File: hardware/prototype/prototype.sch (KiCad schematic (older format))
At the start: 75 parts, among them J1 0734120114, J2 Conn_01x04, J4 Conn_01x04, J5 Conn_02x07_Odd_Even, J6 Battery-holder, J7 Conn_02x12_Odd_Even, J8 Jack-DC, Q1 DTC143Z, Q2 Si2323, U1 QUECTEL_L80, U2 TLV71333PDBV, U3 LM2596_MODULE, U4 DevkitC, U5 MIKROE_3G_CLICK

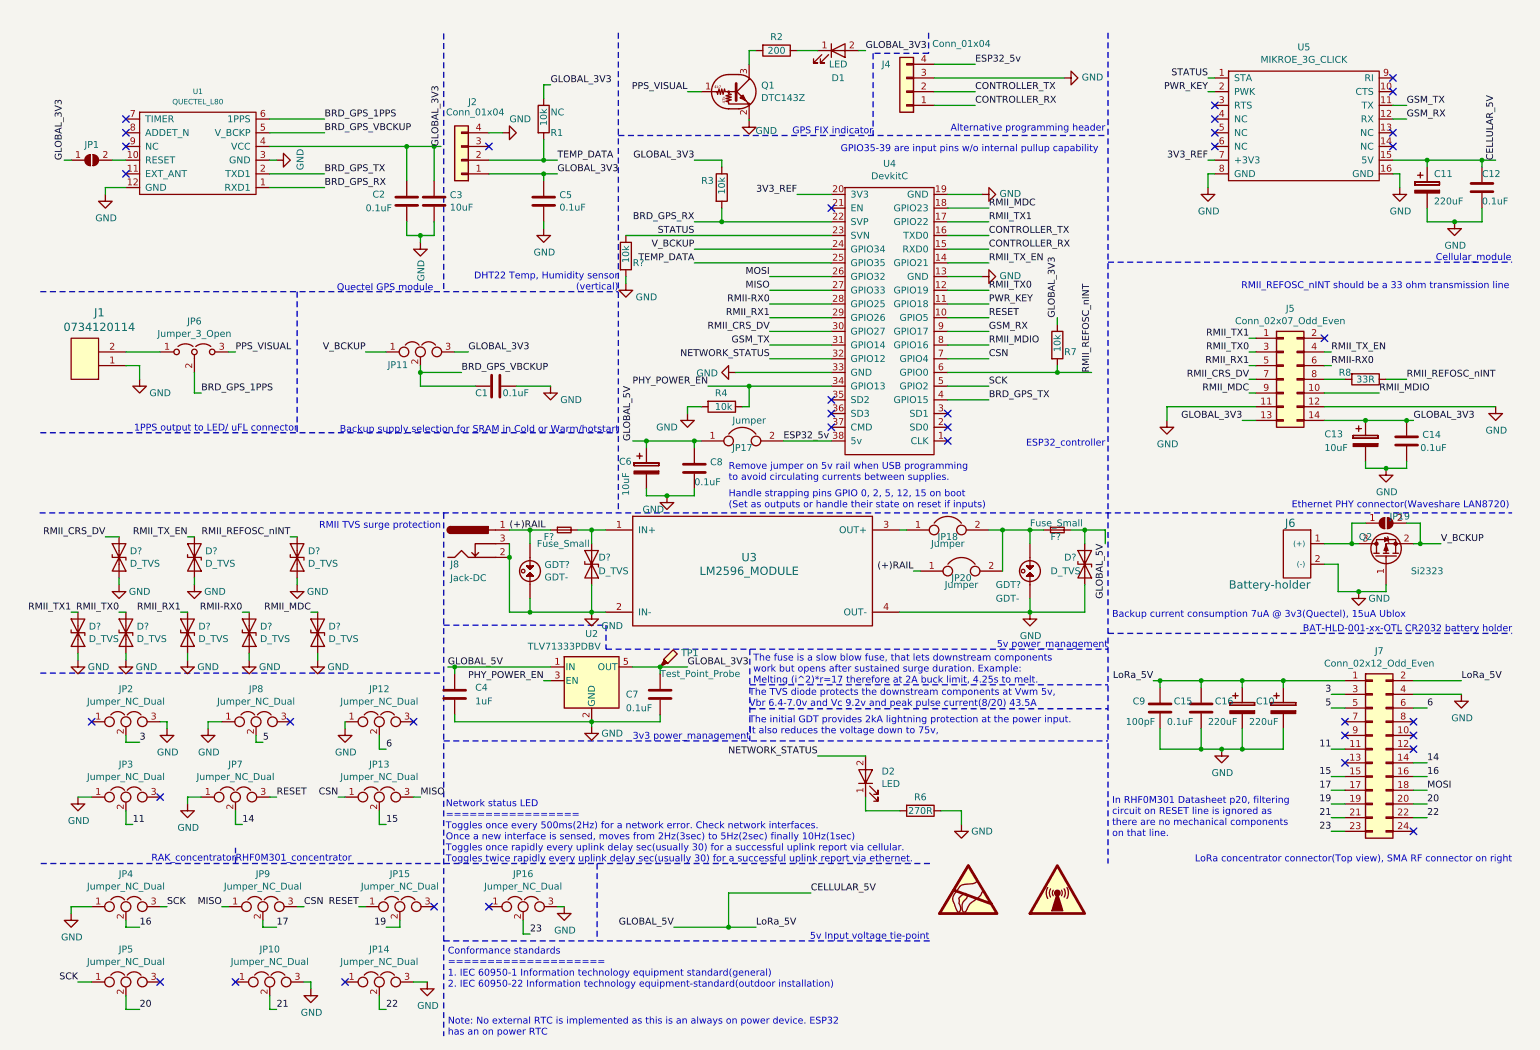
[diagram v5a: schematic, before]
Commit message: Complete schematic and component footpint selection
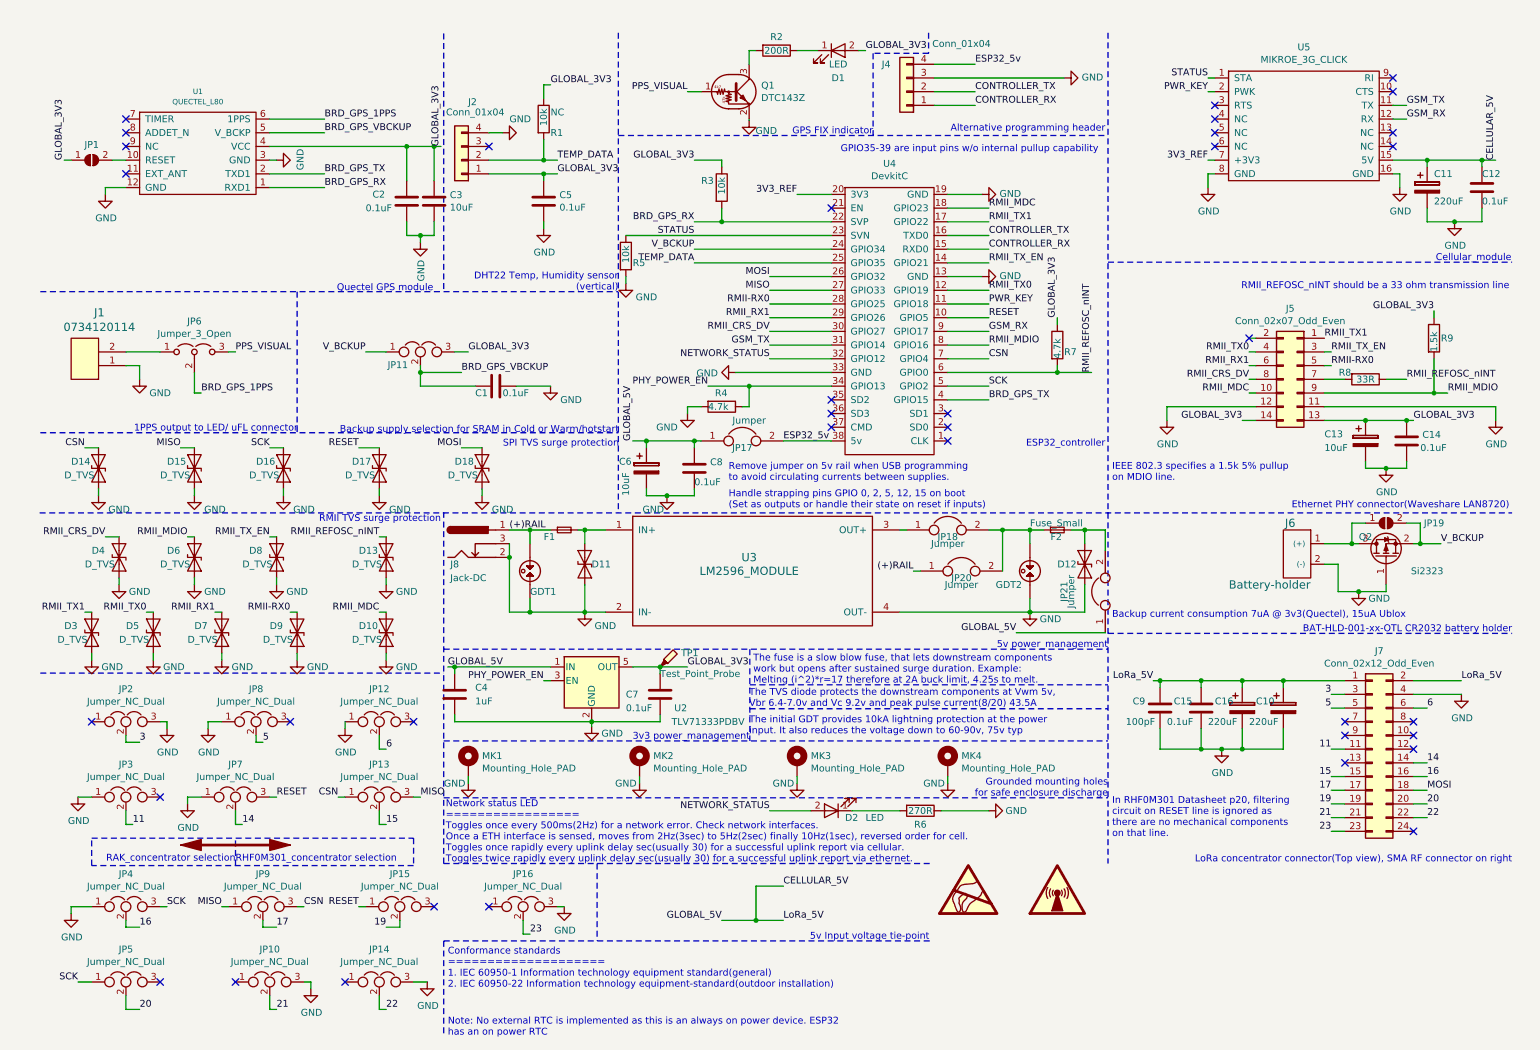
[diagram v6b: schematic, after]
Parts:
- removed D? (x8): D_TVS, symbol Device:D_TVS
- removed GDT?: GDT-, symbol GDT-:GDT-
- added D10, D13, D14, D15, D16, D17, D18, D3, D4, D5, D6, D7, D8, D9: D_TVS, Diode_SMD:D_0402_1005Metric, symbol Device:D_TVS
- added GDT2: GDT-, lib_fp:SL1411A075-SM, symbol GDT-:GDT-
- added JP21: Jumper, Connector_PinSocket_2.54mm:PinSocket_1x02_P2.54mm_Vertical, symbol Device:Jumper
- added MK1, MK2, MK3, MK4: Mounting_Hole_PAD, MountingHole:MountingHole_3.2mm_M3_Pad_Via, symbol Mechanical:Mounting_Hole_PAD
- added R9: 1.5k, Resistor_SMD:R_0805_2012Metric, symbol Device:R
- D11, D12: renamed from D?; footprint (none) -> digikey-footprints:DO-214AC
- F1, F2: renamed from F?; footprint (none) -> lib_fp:461_series_Telelink
- GDT1: renamed from GDT?; footprint (none) -> lib_fp:SL1411A075-SM; purchase page https://www.digikey.com/product-detail/en/littelfuse-inc/SG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 -> https://www.digikey.com/product-detail/en/littelfuse-inc/SL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
- J2: footprint Connector_PinSocket_2.54mm:PinSocket_1x04_P2.54mm_Vertical -> lib_fp:PinHeader_1x04_P2.54mm_staggered_Vertical
- J4: footprint Connector_PinHeader_2.54mm:PinHeader_1x04_P2.54mm_Vertical -> lib_fp:PinHeader_1x04_P2.54mm_staggered_Vertical
- J5: footprint Connector_PinSocket_2.54mm:PinSocket_2x07_P2.54mm_Horizontal -> lib_fp:waveshare_lan_8720
- R2: value 200 -> 200R
- R4, R7: value 10k -> 4.7k
- R5: renamed from R?; footprint (none) -> Resistor_SMD:R_0805_2012Metric
- U5: footprint (none) -> lib_fp:MIKROE_UG95
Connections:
- net CELLULAR_5V: now also JP21.1; no longer D12.1 (A1), F2.2
- net CSN: now also D14.1 (A1)
- net GLOBAL_3V3: now also R9.1
- net GND: now also D10.2 (A2), D13.2 (A2), D14.2 (A2), D15.2 (A2), D16.2 (A2), D17.2 (A2), D18.2 (A2), D3.2 (A2), D4.2 (A2), D5.2 (A2), D6.2 (A2), D7.2 (A2), D8.2 (A2), D9.2 (A2), GDT2.2, MK1.1, MK2.1, MK3.1, MK4.1
- net MISO: now also D15.1 (A1)
- net MOSI: now also D18.1 (A1)
- net RESET: now also D17.1 (A1)
- net RMII-RX0: now also J5.5 (Pin_5), D9.1 (A1); no longer J5.6 (Pin_6)
- net RMII_CRS_DV: now also J5.8 (Pin_8), D4.1 (A1); no longer J5.7 (Pin_7)
- net RMII_MDC: now also J5.10 (Pin_10), D10.1 (A1); no longer J5.9 (Pin_9)
- net RMII_MDIO: now also J5.9 (Pin_9), D6.1 (A1), R9.2; no longer J5.10 (Pin_10)
- net RMII_REFOSC_nINT: now also D13.1 (A1)
- net RMII_RX1: now also J5.6 (Pin_6), D7.1 (A1); no longer J5.5 (Pin_5)
- net RMII_TX0: now also J5.4 (Pin_4), D5.1 (A1); no longer J5.3 (Pin_3)
- net RMII_TX1: now also D3.1 (A1)
- net RMII_TX_EN: now also J5.3 (Pin_3), D8.1 (A1); no longer J5.4 (Pin_4)
- net SCK: now also D16.1 (A1)
- net at F2.1, JP18.2, JP20.2: now also GDT2.1
- net at R8.2: now also J5.7 (Pin_7); no longer J5.8 (Pin_8)
- new net: D12.1 (A1), F2.2, JP21.2
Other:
- note added: "Grounded mounting holes \nfor safe enclosure discharge"
- note added: "IEEE 802.3 specifies a 1.5k 5% pullup \non MDIO line."
- note added: "Network status LED\n=================\nToggles once every 500ms(2Hz) for a network error. Check network interfaces.\nOnce a ETH interface is sensed, moves from 2Hz(3sec) to 5Hz(2sec) finally 10Hz(1sec), reversed order for cell.\nToggles once rapidly every uplink delay sec(usually 30) for a successful uplink report via cellular.\nToggles twice rapidly every uplink delay sec(usually 30) for a succe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"
- note added: "RAK_concentrator selection"
- note added: "RHF0M301_concentrator selection"
- note added: "SPI TVS surge protection"
- note added: "The initial GDT provides 10kA lightning protection at the power \ninput. It also reduces the voltage down to 60-90v, 75v typ"
- note removed: "Network status LED\n=================\nToggles once every 500ms(2Hz) for a network error. Check network interfaces.\nOnce a new interface is sensed, moves from 2Hz(3sec) to 5Hz(2sec) finally 10Hz(1sec)\nToggles once rapidly every uplink delay sec(usually 30) for a successful uplink report via cellular.\nToggles twice rapidly every uplink delay sec(usually 30) for a successful uplink report via et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"
- note removed: "RAK_concentrator"
- note removed: "RHF0M301_concentrator"
- note removed: "The initial GDT provides 2kA lightning protection at the power input.\nIt also reduces the voltage down to 75v,"
- moved on the sheet: D11, D2

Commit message: Layout part of the components
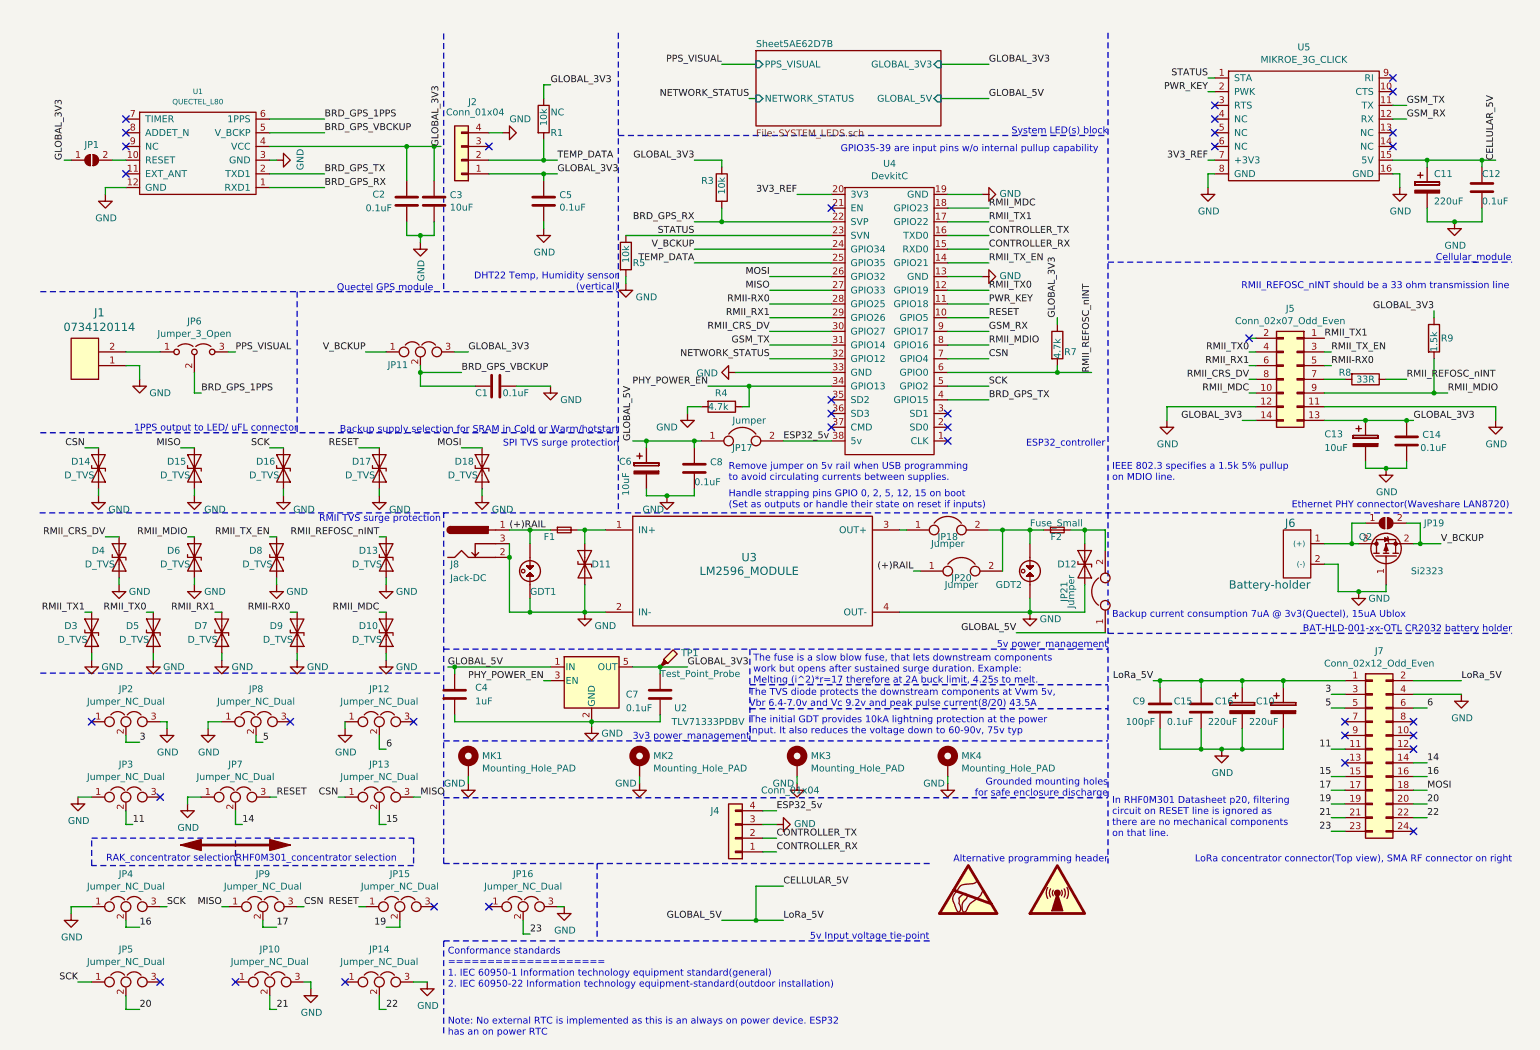
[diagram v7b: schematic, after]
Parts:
- removed D1, D2: LED, LED_SMD:LED_0805_2012Metric_Pad0.97x1.50mm_HandSolder, symbol Device:LED
- removed Q1: DTC143Z, Package_TO_SOT_SMD:SC-59_Handsoldering, symbol Transistor_BJT:DTC143Z
- removed R2: 200R, Resistor_SMD:R_0805_2012Metric, symbol Device:R
- removed R6: 270R, Resistor_SMD:R_0805_2012Metric, symbol Device:R
- J5: footprint lib_fp:waveshare_lan_8720 -> lib_fp:lan_waveshare_8720
- JP10, JP11, JP12, JP13, JP14, JP15, JP16, JP2, JP3, JP4, JP5, JP6, JP7, JP8, JP9: footprint Connector_PinHeader_2.54mm:PinHeader_1x03_P2.54mm_Vertical -> lib_fp:PinHeader_1x03_P2.54mm_staggered_Vertical
- JP17, JP18, JP20, JP21: footprint Connector_PinSocket_2.54mm:PinSocket_1x02_P2.54mm_Vertical -> lib_fp:PinHeader_1x02_P2.54mm_staggered_Vertical
- Q2: footprint TO_SOT_Packages_SMD:SOT-23 -> Package_TO_SOT_SMD:SOT-23
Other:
- note added: "System LED(s) block"
- note removed: "GPS FIX indicator"
- note removed: "Network status LED\n=================\nToggles once every 500ms(2Hz) for a network error. Check network interfaces.\nOnce a ETH interface is sensed, moves from 2Hz(3sec) to 5Hz(2sec) finally 10Hz(1sec), reversed order for cell.\nToggles once rapidly every uplink delay sec(usually 30) for a successful uplink report via cellular.\nToggles twice rapidly every uplink delay sec(usually 30) for a succe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"
- moved on the sheet: J4

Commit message: Complete PCB layout
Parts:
- removed D10, D13, D14, D15, D16, D17, D18, D3, D4, D5, D6, D7, D8, D9: D_TVS, Diode_SMD:D_0402_1005Metric, symbol Device:D_TVS
- removed JP20: Jumper, lib_fp:PinHeader_1x02_P2.54mm_staggered_Vertical, symbol Device:Jumper
- removed TP1: Test_Point_Probe, TestPoint:TestPoint_Pad_D1.0mm, symbol Connector_Specialized:Test_Point_Probe
- added JP11: Jumper_NC_Dual, lib_fp:PinHeader_1x03_P2.54mm_staggered_Vertical, symbol Device:Jumper_NC_Dual
- renumbered C2 to C1, C15 to C10, C16 to C11, C10 to C12, C11 to C15, C12 to C16, C3 to C2, C4 to C3, C1 to C4, D11 to D1, D12 to D2, J8 to J1, J1 to J2, J2 to J3, JP11 to JP16, JP16 to JP17, JP17 to JP18, JP18 to JP19, JP21 to JP20, JP19 to JP21, Q2 to Q1, R5 to R2, R7 to R5, R8 to R6, R9 to R7
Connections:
- net CELLULAR_5V: now also JP20.2; no longer JP20.1
- net 5v_rail: now reaches F2.1, GDT2.1, JP19.2
- net 5v_rail: now also JP11.3
- net at D2.1 (A1), F2.2: now also JP20.1; no longer JP20.2
- net (+)RAIL renamed 12v_rail
- net 12v_rail: now also JP11.1; no longer J1.1
- new net Power_Input: J1.1, JP11.2
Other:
- note added: "Power_management"
- note added: "Protection on the LAN8720A RMII interface is implemented in die with HBM\nESD performance of class 3A(4kv-8kv), no need for external protection"
- note added: "Protection on the SX1301 SPI interface is implemented in die with a \nHBM ESD performance of class 2(2kv-4kv), no need for external protection"
- note removed: "5v power_management"
- note removed: "RMII TVS surge protection"
- note removed: "SPI TVS surge protection"
- moved on the sheet: D1, D2, F1, F2, GDT1, GDT2, J1, JP19, JP20, U3
